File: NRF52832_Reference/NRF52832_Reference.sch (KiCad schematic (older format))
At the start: 50 parts

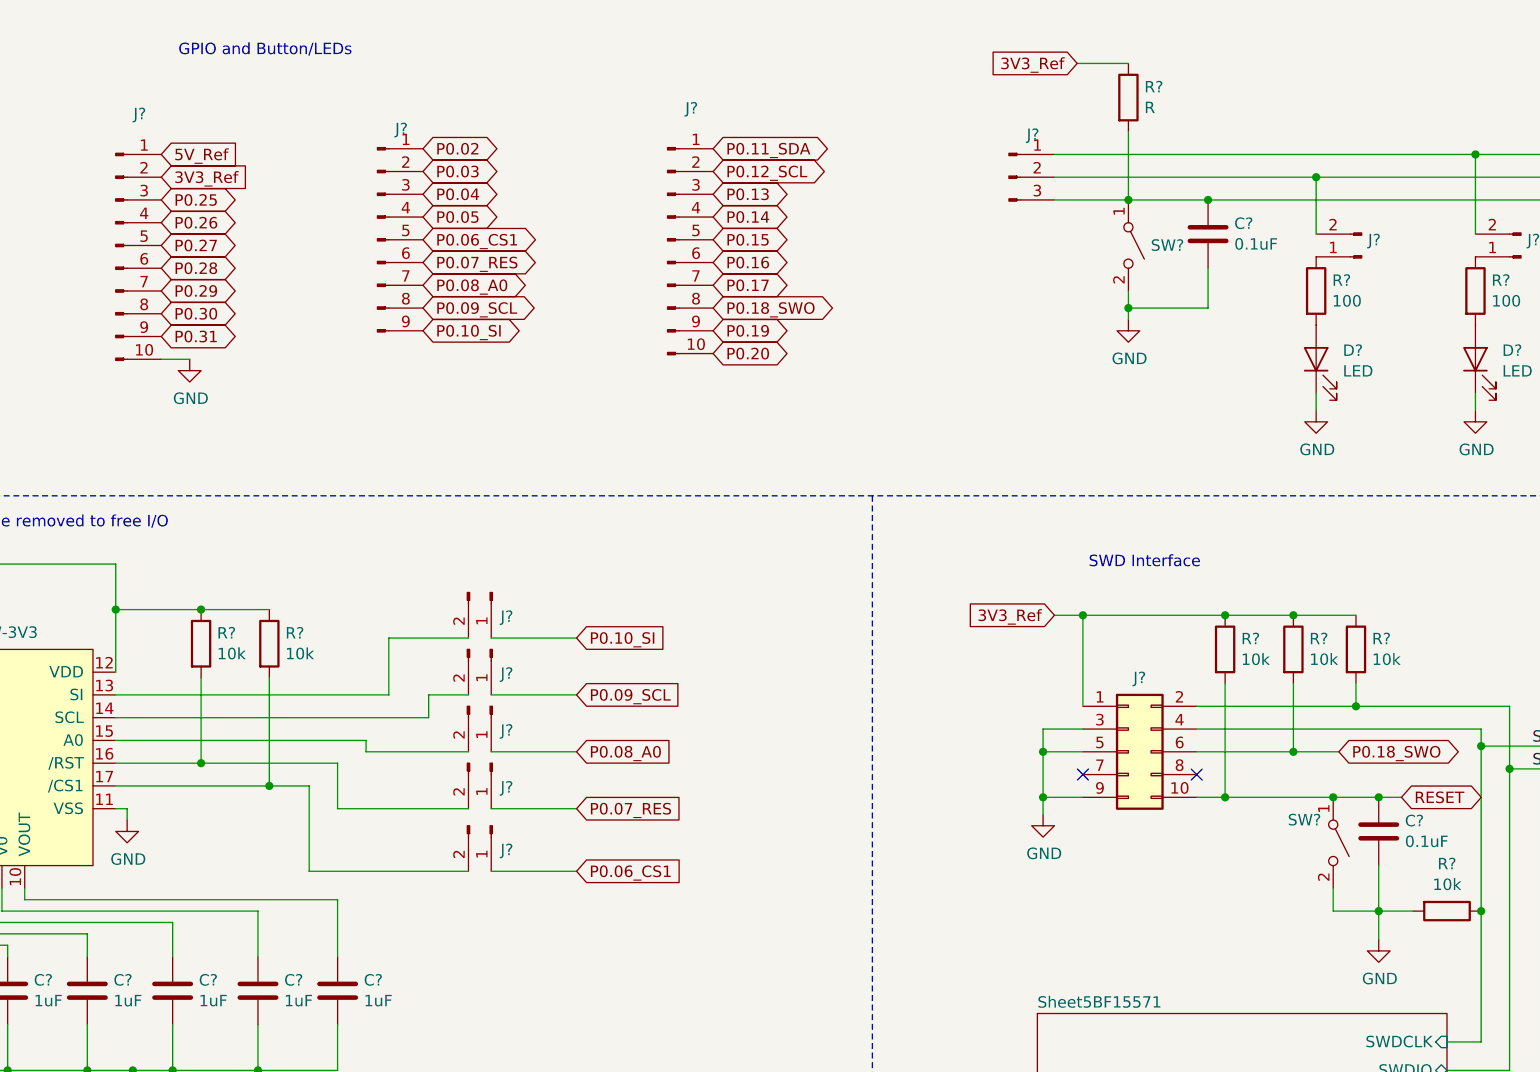
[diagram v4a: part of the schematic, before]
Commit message: Finished foorprint assignments for GPIO pins, LEDs, and button.
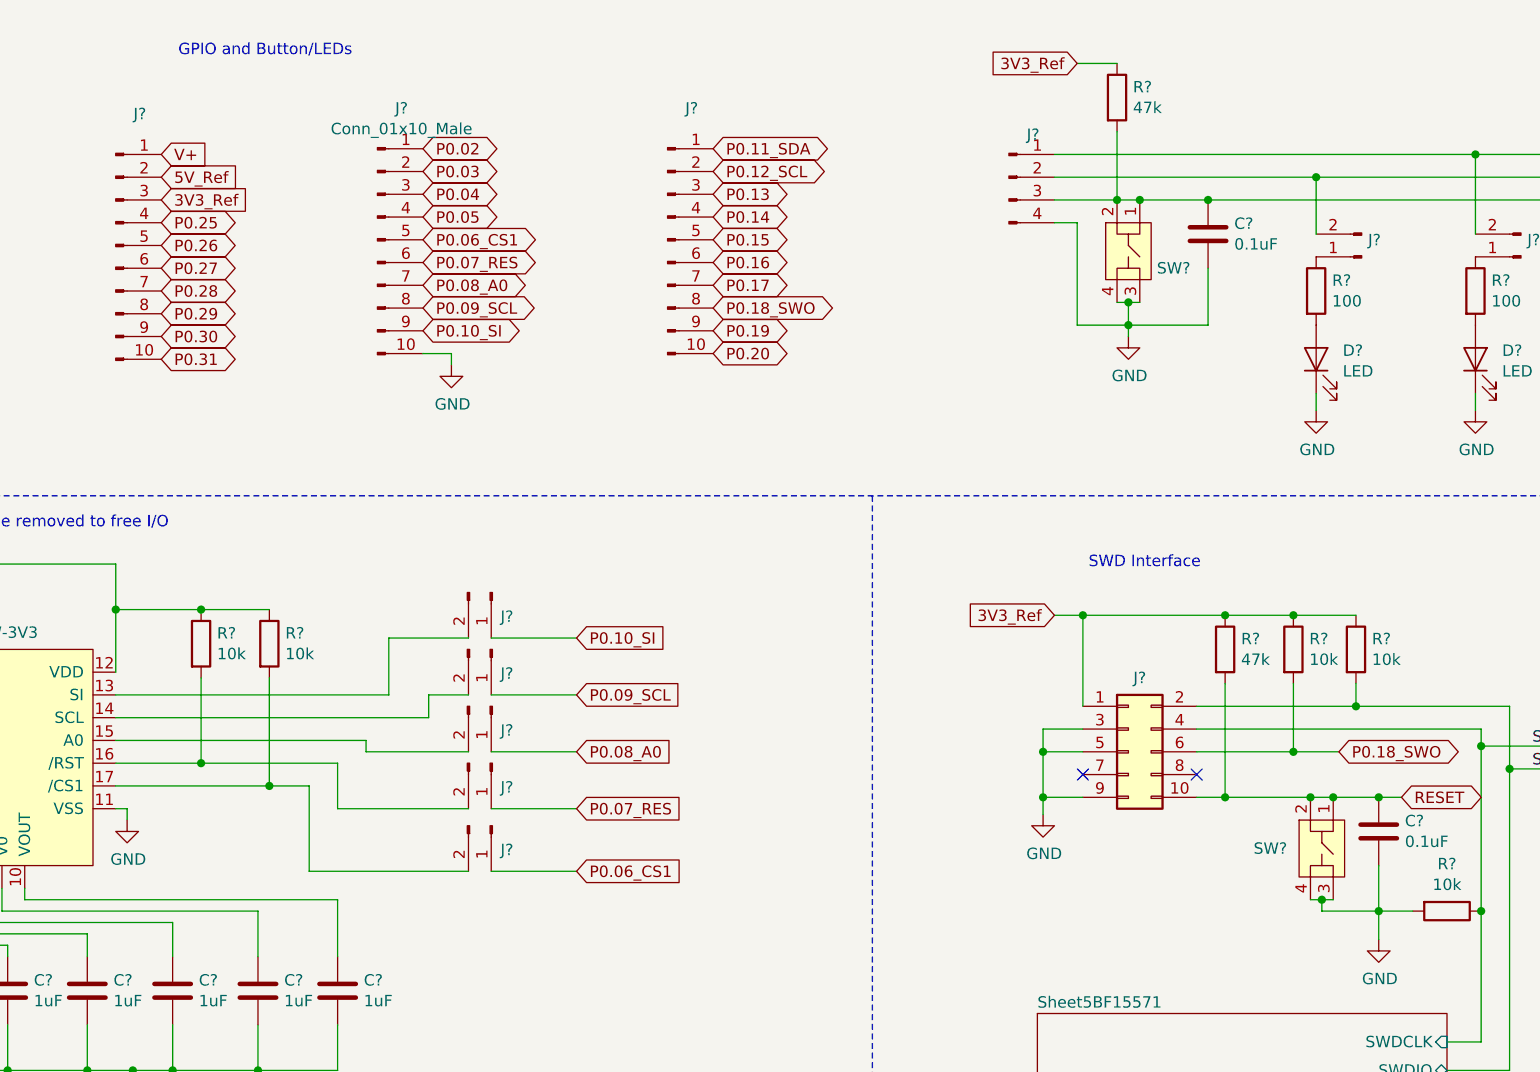
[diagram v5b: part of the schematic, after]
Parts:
- removed J?: Conn_01x09_Male, symbol Connector:Conn_01x09_Male
- removed J?: Conn_01x03_Male, symbol Connector:Conn_01x03_Male
- removed SW? (x2): SW_SPST, symbol Switch:SW_SPST
- added J?: Conn_01x04_Male, Connector_PinHeader_2.54mm:PinHeader_1x04_P2.54mm_Vertical, symbol Connector:Conn_01x04_Male
- added J?: Conn_01x10_Male, Connector_PinHeader_2.54mm:PinHeader_1x10_P2.54mm_Vertical, symbol Connector:Conn_01x10_Male
- added SW? (x2): SW_SPST_4pin, Custom_Footprints:SW_Tactile_TE_1825910-6, symbol Project_Libary:SW_SPST_4pin
- C?: footprint (none) -> Capacitor_SMD:C_0603_1608Metric_Pad1.05x0.95mm_HandSolder
- D? (x2): footprint (none) -> LED_SMD:LED_0603_1608Metric_Pad1.05x0.95mm_HandSolder
- J? (x2): footprint (none) -> Connector_PinHeader_2.54mm:PinHeader_1x10_P2.54mm_Vertical
- J? (x2): footprint (none) -> Connector_PinHeader_2.54mm:PinHeader_1x02_P2.54mm_Vertical
- R?: value 10k -> 47k
- R?: value R -> 47k; footprint (none) -> Resistor_SMD:R_0603_1608Metric_Pad1.05x0.95mm_HandSolder
- R? (x2): footprint (none) -> Resistor_SMD:R_0603_1608Metric_Pad1.05x0.95mm_HandSolder
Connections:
- net 3V3_Ref: now also J?.3 (Pin_3); no longer J?.2 (Pin_2)
- net 5V_Ref: now also J?.2 (Pin_2); no longer J?.1 (Pin_1)
- net GND: now also J?.10 (Pin_10), J?.4 (Pin_4), SW?.3, SW?.3, SW?.4, SW?.4; no longer J?.10 (Pin_10)
- net P0.02: now also J?.1 (Pin_1)
- net P0.03: now also J?.2 (Pin_2)
- net P0.04: now also J?.3 (Pin_3)
- net P0.05: now also J?.4 (Pin_4)
- net P0.06_CS1: now also J?.5 (Pin_5)
- net P0.07_RES: now also J?.6 (Pin_6)
- net P0.08_A0: now also J?.7 (Pin_7)
- net P0.09_SCL: now also J?.8 (Pin_8)
- net P0.10_SI: now also J?.9 (Pin_9)
- net P0.22: now also J?.1 (Pin_1)
- net P0.23: now also J?.2 (Pin_2)
- net P0.24: now also J?.3 (Pin_3), SW?.1, SW?.2
- net P0.25: now also J?.4 (Pin_4); no longer J?.3 (Pin_3)
- net P0.26: now also J?.5 (Pin_5); no longer J?.4 (Pin_4)
- net P0.27: now also J?.6 (Pin_6); no longer J?.5 (Pin_5)
- net P0.28: now also J?.7 (Pin_7); no longer J?.6 (Pin_6)
- net P0.29: now also J?.8 (Pin_8); no longer J?.7 (Pin_7)
- net P0.30: now also J?.9 (Pin_9); no longer J?.8 (Pin_8)
- net P0.31: now also J?.10 (Pin_10); no longer J?.9 (Pin_9)
- net RESET: now also SW?.1, SW?.2
- new net V+: J?.1 (Pin_1)
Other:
- moved on the sheet: R?
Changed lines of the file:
@@
 F 0 "J?" H 3731 2053 50  0000 C CNN
 F 1 "Conn_01x10_Male" H 3731 1962 50  0001 C CNN
-F 2 "" H 3625 1475 50  0001 C CNN
+F 2 "Connector_PinHeader_2.54mm:PinHeader_1x10_P2.54mm_Vertical" H 3625 1475 50  0001 C CNN
 F 3 "~" H 3625 1475 50  0001 C CNN
 	1    3625 1475
@@
 F 0 "J?" H 6156 2028 50  0000 C CNN
 F 1 "Conn_01x10_Male" H 6156 1937 50  0001 C CNN
-F 2 "" H 6050 1450 50  0001 C CNN
+F 2 "Connector_PinHeader_2.54mm:PinHeader_1x10_P2.54mm_Vertical" H 6050 1450 50  0001 C CNN
 F 3 "~" H 6050 1450 50  0001 C CNN
 	1    6050 1450
@@
 P 8500 3250
 F 0 "R?" H 8570 3296 50  0000 L CNN
-F 1 "10k" H 8570 3205 50  0000 L CNN
+F 1 "47k" H 8570 3205 50  0000 L CNN
 F 2 "" V 8430 3250 50  0001 C CNN
 F 3 "~" H 8500 3250 50  0001 C CNN
 	1    8500 3250
 	1    0    0    -1
-$EndComp
-$Comp
-L Switch:SW_SPST SW?
-U 1 1 5C0A6C29
-P 8975 4100
-F 0 "SW?" V 8875 3900 50  0000 L CNN
-F 1 "SW_SPST" V 9020 4198 50  0001 L CNN
-F 2 "" H 8975 4100 50  0001 C CNN
-F 3 "" H 8975 4100 50  0001 C CNN
-	1    8975 4100
-	0    1    1    0
 $EndComp
 $Comp
@@
 	1    0    0    -1
 $EndComp
-Connection ~ 8975 3900
-Wire Wire Line
-	8975 3900 9175 3900
 Connection ~ 9175 3900
 Wire Wire Line
 	9175 3900 9275 3900
-Wire Wire Line
-	8975 4400 9175 4400
 Wire Wire Line
 	9175 4400 9175 4525
@@
 Connection ~ 8500 3100
 Connection ~ 8500 3900
-Wire Wire Line
-	8500 3900 8975 3900
 Connection ~ 8800 3100
 Wire Wire Line
@@
 Wire Wire Line
 	5650 4225 5275 4225
-Text GLabel 3825 1075 2    50   Input ~ 0
+Text GLabel 3825 1175 2    50   Input ~ 0
 5V_Ref
-Text GLabel 3825 1175 2    50   Input ~ 0
+Text GLabel 3825 1275 2    50   Input ~ 0
 3V3_Ref
-$Comp
-L power:GND #PWR?
-U 1 1 5C235D31
-P 3950 1975
-F 0 "#PWR?" H 3950 1725 50  0001 C CNN
-F 1 "GND" H 3955 1802 50  0000 C CNN
-F 2 "" H 3950 1975 50  0001 C CNN
-F 3 "" H 3950 1975 50  0001 C CNN
-	1    3950 1975
-	1    0    0    -1
-$EndComp
-Text GLabel 3825 1275 2    50   BiDi ~ 0
+Text GLabel 3825 1375 2    50   BiDi ~ 0
 P0.25
-Text GLabel 3825 1375 2    50   BiDi ~ 0
+Text GLabel 3825 1475 2    50   BiDi ~ 0
 P0.26
-Text GLabel 3825 1475 2    50   BiDi ~ 0
+Text GLabel 3825 1575 2    50   BiDi ~ 0
 P0.27
-Text GLabel 3825 1575 2    50   BiDi ~ 0
+Text GLabel 3825 1675 2    50   BiDi ~ 0
 P0.28
-Text GLabel 3825 1675 2    50   BiDi ~ 0
+Text GLabel 3825 1775 2    50   BiDi ~ 0
 P0.29
-Text GLabel 3825 1775 2    50   BiDi ~ 0
+Text GLabel 3825 1875 2    50   BiDi ~ 0
 P0.30
-Text GLabel 3825 1875 2    50   BiDi ~ 0
+Text GLabel 3825 1975 2    50   BiDi ~ 0
 P0.31
-Wire Wire Line
-	3950 1975 3825 1975
 Text Notes 1200 2725 0    50   ~ 0
 LCD Display using SPI interface. Has jumpers that can be removed to free I/O
 Wire Notes Line
 	6950 2575 6950 7775
-$Comp
-L Connector:Conn_01x09_Male J?
-U 1 1 5C25D3E9
-P 4775 1450
-F 0 "J?" H 4881 1937 50  0000 C CNN
-F 1 "Conn_01x09_Male" H 4881 1937 50  0001 C CNN
-F 2 "" H 4775 1450 50  0001 C CNN
-F 3 "~" H 4775 1450 50  0001 C CNN
-	1    4775 1450
-	1    0    0    -1
-$EndComp
 Text GLabel 4975 1050 2    50   BiDi ~ 0
 P0.02
@@
 P0.20
 $Comp
-L Connector:Conn_01x03_Male J?
-U 1 1 5C282C46
-P 7550 1175
-F 0 "J?" H 7656 1362 50  0000 C CNN
-F 1 "Conn_01x03_Male" H 7656 1362 50  0001 C CNN
-F 2 "" H 7550 1175 50  0001 C CNN
-F 3 "~" H 7550 1175 50  0001 C CNN
-	1    7550 1175
-	1    0    0    -1
-$EndComp
-$Comp
-L Switch:SW_SPST SW?
-U 1 1 5C28371C
-P 8075 1475
-F 0 "SW?" V 8075 1573 50  0000 L CNN
-F 1 "SW_SPST" V 8120 1573 50  0001 L CNN
-F 2 "" H 8075 1475 50  0001 C CNN
-F 3 "" H 8075 1475 50  0001 C CNN
-	1    8075 1475
-	0    1    1    0
-$EndComp
-$Comp
 L Device:R R?
 U 1 1 5C2838F9
-P 8075 825
-F 0 "R?" H 8145 871 50  0000 L CNN
-F 1 "R" H 8145 780 50  0000 L CNN
-F 2 "" V 8005 825 50  0001 C CNN
-F 3 "~" H 8075 825 50  0001 C CNN
-	1    8075 825
+P 8025 825
+F 0 "R?" H 8095 871 50  0000 L CNN
+F 1 "47k" H 8095 780 50  0000 L CNN
+F 2 "Resistor_SMD:R_0603_1608Metric_Pad1.05x0.95mm_HandSolder" V 7955 825 50  0001 C CNN
+F 3 "~" H 8025 825 50  0001 C CNN
+	1    8025 825
 	1    0    0    -1
 $EndComp
@@
 F 0 "C?" H 8540 1471 50  0000 L CNN
 F 1 "0.1uF" H 8540 1380 50  0000 L CNN
-F 2 "" H 8463 1275 50  0001 C CNN
+F 2 "Capacitor_SMD:C_0603_1608Metric_Pad1.05x0.95mm_HandSolder" H 8463 1275 50  0001 C CNN
 F 3 "~" H 8425 1425 50  0001 C CNN
 	1    8425 1425
@@
 F 0 "R?" H 8970 1721 50  0000 L CNN
 F 1 "100" H 8970 1630 50  0000 L CNN
-F 2 "" V 8830 1675 50  0001 C CNN
+F 2 "Resistor_SMD:R_0603_1608Metric_Pad1.05x0.95mm_HandSolder" V 8830 1675 50  0001 C CNN
 F 3 "~" H 8900 1675 50  0001 C CNN
 	1    8900 1675
@@
 F 0 "R?" H 9670 1721 50  0000 L CNN
 F 1 "100" H 9670 1630 50  0000 L CNN
-F 2 "" V 9530 1675 50  0001 C CNN
+F 2 "Resistor_SMD:R_0603_1608Metric_Pad1.05x0.95mm_HandSolder" V 9530 1675 50  0001 C CNN
 F 3 "~" H 9600 1675 50  0001 C CNN
 	1    9600 1675
@@
 F 0 "D?" V 8938 1858 50  0000 R CNN
 F 1 "LED" V 8847 1858 50  0000 R CNN
-F 2 "" H 8900 1975 50  0001 C CNN
+F 2 "LED_SMD:LED_0603_1608Metric_Pad1.05x0.95mm_HandSolder" H 8900 1975 50  0001 C CNN
 F 3 "~" H 8900 1975 50  0001 C CNN
 	1    8900 1975
@@
 F 0 "D?" V 9638 1858 50  0000 R CNN
 F 1 "LED" V 9547 1858 50  0000 R CNN
-F 2 "" H 9600 1975 50  0001 C CNN
+F 2 "LED_SMD:LED_0603_1608Metric_Pad1.05x0.95mm_HandSolder" H 9600 1975 50  0001 C CNN
 F 3 "~" H 9600 1975 50  0001 C CNN
 	1    9600 1975
@@
 F 0 "J?" H 9072 1451 50  0000 R CNN
 F 1 "Conn_01x02_Male" H 9206 1612 50  0001 C CNN
-F 2 "" H 9100 1525 50  0001 C CNN
+F 2 "Connector_PinHeader_2.54mm:PinHeader_1x02_P2.54mm_Vertical" H 9100 1525 50  0001 C CNN
 F 3 "~" H 9100 1525 50  0001 C CNN
 	1    9100 1525
@@
 F 0 "J?" H 9772 1451 50  0000 R CNN
 F 1 "Conn_01x02_Male" H 9906 1612 50  0001 C CNN
-F 2 "" H 9800 1525 50  0001 C CNN
+F 2 "Connector_PinHeader_2.54mm:PinHeader_1x02_P2.54mm_Vertical" H 9800 1525 50  0001 C CNN
 F 3 "~" H 9800 1525 50  0001 C CNN
 	1    9800 1525
@@
 Wire Wire Line
 	10050 1275 8425 1275
-Connection ~ 8075 1275
-Wire Wire Line
-	8075 1275 7750 1275
 Connection ~ 8425 1275
-Wire Wire Line
-	8425 1275 8075 1275
 Wire Wire Line
 	8900 1425 8900 1175
@@
 	9600 1075 7750 1075
 Wire Wire Line
-	8075 1275 8075 975
-Wire Wire Line
-	8075 675  7850 675
+	8025 1275 8025 975
 $Comp
 L power:GND #PWR?
 U 1 1 5C307A22
-P 8075 1800
-F 0 "#PWR?" H 8075 1550 50  0001 C CNN
-F 1 "GND" H 8080 1627 50  0000 C CNN
-F 2 "" H 8075 1800 50  0001 C CNN
-F 3 "" H 8075 1800 50  0001 C CNN
-	1    8075 1800
+P 8075 1875
+F 0 "#PWR?" H 8075 1625 50  0001 C CNN
+F 1 "GND" H 8080 1702 50  0000 C CNN
+F 2 "" H 8075 1875 50  0001 C CNN
+F 3 "" H 8075 1875 50  0001 C CNN
+	1    8075 1875
 	1    0    0    -1
 $EndComp
@@
 	1    0    0    -1
 $EndComp
-Wire Wire Line
-	8075 1675 8075 1750
-Wire Wire Line
-	8425 1575 8425 1750
-Wire Wire Line
-	8425 1750 8075 1750
-Connection ~ 8075 1750
-Wire Wire Line
-	8075 1750 8075 1800
 Wire Wire Line
 	8900 2125 8900 2200
@@
 	9625 3675 9625 4400
 Wire Wire Line
-	8975 4400 8975 4300
-Wire Wire Line
 	9175 4200 9175 4400
+Text GLabel 3825 1075 2    50   Input ~ 0
+V+
+$Comp
+L Connector:Conn_01x04_Male J?
+U 1 1 5C11D05F
+P 7550 1175
+F 0 "J?" H 7656 1362 50  0000 C CNN
+F 1 "Conn_01x04_Male" H 7656 1362 50  0001 C CNN
+F 2 "Connector_PinHeader_2.54mm:PinHeader_1x04_P2.54mm_Vertical" H 7550 1175 50  0001 C CNN
+F 3 "~" H 7550 1175 50  0001 C CNN
+	1    7550 1175
+	1    0    0    -1
+$EndComp
+$Comp
+L Connector:Conn_01x10_Male J?
+U 1 1 5C127DBC
+P 4775 1450
+F 0 "J?" H 4881 2028 50  0000 C CNN
+F 1 "Conn_01x10_Male" H 4881 1937 50  0000 C CNN
+F 2 "Connector_PinHeader_2.54mm:PinHeader_1x10_P2.54mm_Vertical" H 4775 1450 50  0001 C CNN
+F 3 "~" H 4775 1450 50  0001 C CNN
+	1    4775 1450
+	1    0    0    -1
+$EndComp
+$Comp
+L power:GND #PWR?
+U 1 1 5C127EF2
+P 5100 2000
+F 0 "#PWR?" H 5100 1750 50  0001 C CNN
+F 1 "GND" H 5105 1827 50  0000 C CNN
+F 2 "" H 5100 2000 50  0001 C CNN
+F 3 "" H 5100 2000 50  0001 C CNN
+	1    5100 2000
+	1    0    0    -1
+$EndComp
+Wire Wire Line
+	4975 1950 5100 1950
+Wire Wire Line
+	5100 1950 5100 2000
+Connection ~ 8025 1275
+Wire Wire Line
+	8025 675  7850 675
+Wire Wire Line
+	8025 1725 8075 1725
+Wire Wire Line
+	8075 1725 8075 1825
+Connection ~ 8075 1725
+Wire Wire Line
+	8425 1825 8075 1825
+Wire Wire Line
+	8425 1575 8425 1825
+Connection ~ 8075 1825
+Wire Wire Line
+	8075 1825 8075 1875
+Wire Wire Line
+	7750 1375 7850 1375
+Wire Wire Line
+	7850 1375 7850 1825
+Wire Wire Line
+	7850 1825 8075 1825
+Wire Wire Line
+	8875 4350 8925 4350
+Wire Wire Line
+	8925 4350 8925 4400
+Wire Wire Line
+	8925 4400 9175 4400
+Connection ~ 8925 4350
+Wire Wire Line
+	8925 4350 8975 4350
+Wire Wire Line
+	8500 3900 8875 3900
+$Comp
+L Project_Libary:SW_SPST_4pin SW?
+U 1 1 5C1A448E
+P 8075 1575
+F 0 "SW?" V 8075 1700 50  0000 L CNN
+F 1 "SW_SPST_4pin" V 8045 1713 50  0001 L CNN
+F 2 "Custom_Footprints:SW_Tactile_TE_1825910-6" H 8125 1775 50  0001 C CNN
+F 3 "" H 8125 1775 50  0001 C CNN
+	1    8075 1575
+	0    1    1    0
+$EndComp
+Connection ~ 8125 1275
+Wire Wire Line
+	8125 1275 8425 1275
+$Comp
+L Project_Libary:SW_SPST_4pin SW?
+U 1 1 5C1A47AD
+P 8925 4200
+F 0 "SW?" V 8850 3900 50  0000 L CNN
+F 1 "SW_SPST_4pin" V 8895 4338 50  0001 L CNN
+F 2 "Custom_Footprints:SW_Tactile_TE_1825910-6" H 8975 4400 50  0001 C CNN
+F 3 "" H 8975 4400 50  0001 C CNN
+	1    8925 4200
+	0    1    1    0
+$EndComp
+Wire Wire Line
+	8975 3900 9175 3900
+Wire Wire Line
+	8975 3900 8875 3900
+Wire Wire Line
+	7750 1275 8025 1275
+Wire Wire Line
+	8025 1275 8125 1275
+Wire Wire Line
+	8075 1725 8125 1725
+Connection ~ 8975 3900
+Connection ~ 8875 3900
 $EndSCHEMATC

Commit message: Finished footprint assignment for SWD Header and Reset button
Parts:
- C?: footprint (none) -> Capacitor_SMD:C_0603_1608Metric_Pad1.05x0.95mm_HandSolder
- J?: value Conn_02x05_Odd_Even -> SWD_Header; footprint (none) -> Custom_Footprints:SWD_Header_CNC_Tech_3220-10-0100-00
- J?: footprint (none) -> Connector_PinHeader_2.54mm:PinHeader_1x02_P2.54mm_Vertical
- R? (x4): footprint (none) -> Resistor_SMD:R_0603_1608Metric_Pad1.05x0.95mm_HandSolder
- SW? (x2): value SW_SPST_4pin -> Button
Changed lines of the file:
@@
 F 0 "R?" H 8570 3296 50  0000 L CNN
 F 1 "47k" H 8570 3205 50  0000 L CNN
-F 2 "" V 8430 3250 50  0001 C CNN
+F 2 "Resistor_SMD:R_0603_1608Metric_Pad1.05x0.95mm_HandSolder" V 8430 3250 50  0001 C CNN
 F 3 "~" H 8500 3250 50  0001 C CNN
 	1    8500 3250
@@
 F 0 "C?" H 9290 4096 50  0000 L CNN
 F 1 "0.1uF" H 9290 4005 50  0000 L CNN
-F 2 "" H 9213 3900 50  0001 C CNN
+F 2 "Capacitor_SMD:C_0603_1608Metric_Pad1.05x0.95mm_HandSolder" H 9213 3900 50  0001 C CNN
 F 3 "~" H 9175 4050 50  0001 C CNN
 	1    9175 4050
@@
 P 8075 3700
 F 0 "J?" H 8125 4025 50  0000 C CNN
-F 1 "Conn_02x05_Odd_Even" H 8125 4026 50  0001 C CNN
-F 2 "" H 8075 3700 50  0001 C CNN
+F 1 "SWD_Header" H 8125 4026 50  0001 C CNN
+F 2 "Custom_Footprints:SWD_Header_CNC_Tech_3220-10-0100-00" H 8075 3700 50  0001 C CNN
 F 3 "~" H 8075 3700 50  0001 C CNN
 	1    8075 3700
@@
 F 0 "R?" H 8870 3296 50  0000 L CNN
 F 1 "10k" H 8870 3205 50  0000 L CNN
-F 2 "" V 8730 3250 50  0001 C CNN
+F 2 "Resistor_SMD:R_0603_1608Metric_Pad1.05x0.95mm_HandSolder" V 8730 3250 50  0001 C CNN
 F 3 "~" H 8800 3250 50  0001 C CNN
 	1    8800 3250
@@
 F 0 "R?" H 9145 3296 50  0000 L CNN
 F 1 "10k" H 9145 3205 50  0000 L CNN
-F 2 "" V 9005 3250 50  0001 C CNN
+F 2 "Resistor_SMD:R_0603_1608Metric_Pad1.05x0.95mm_HandSolder" V 9005 3250 50  0001 C CNN
 F 3 "~" H 9075 3250 50  0001 C CNN
 	1    9075 3250
@@
 F 0 "R?" V 9268 4400 50  0000 C CNN
 F 1 "10k" V 9359 4400 50  0000 C CNN
-F 2 "" V 9405 4400 50  0001 C CNN
+F 2 "Resistor_SMD:R_0603_1608Metric_Pad1.05x0.95mm_HandSolder" V 9405 4400 50  0001 C CNN
 F 3 "~" H 9475 4400 50  0001 C CNN
 	1    9475 4400
@@
 F 0 "J?" H 10447 3701 50  0000 R CNN
 F 1 "Conn_01x02_Male" H 10448 3746 50  0001 R CNN
-F 2 "" H 10475 3775 50  0001 C CNN
+F 2 "Connector_PinHeader_2.54mm:PinHeader_1x02_P2.54mm_Vertical" H 10475 3775 50  0001 C CNN
 F 3 "~" H 10475 3775 50  0001 C CNN
 	1    10475 3775
@@
 P 8075 1575
 F 0 "SW?" V 8075 1700 50  0000 L CNN
-F 1 "SW_SPST_4pin" V 8045 1713 50  0001 L CNN
+F 1 "Button" V 8045 1713 50  0001 L CNN
 F 2 "Custom_Footprints:SW_Tactile_TE_1825910-6" H 8125 1775 50  0001 C CNN
 F 3 "" H 8125 1775 50  0001 C CNN
@@
 P 8925 4200
 F 0 "SW?" V 8850 3900 50  0000 L CNN
-F 1 "SW_SPST_4pin" V 8895 4338 50  0001 L CNN
+F 1 "Button" V 8895 4338 50  0001 L CNN
 F 2 "Custom_Footprints:SW_Tactile_TE_1825910-6" H 8975 4400 50  0001 C CNN
 F 3 "" H 8975 4400 50  0001 C CNN
